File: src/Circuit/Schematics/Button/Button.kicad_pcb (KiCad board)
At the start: 2 copper layers, 17 x 15 mm, 5 parts, among them K1 CONN_3, SW1 SW_PUSH

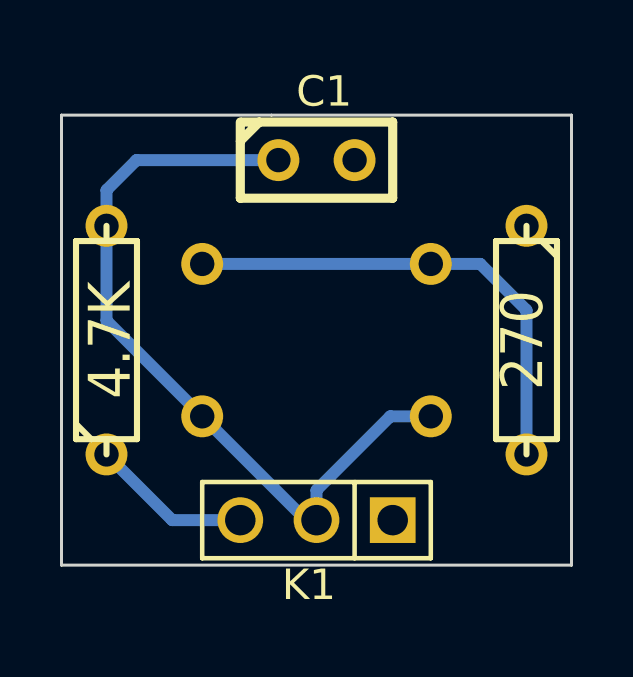
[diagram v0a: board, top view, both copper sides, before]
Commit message: Initial LED driver circuit
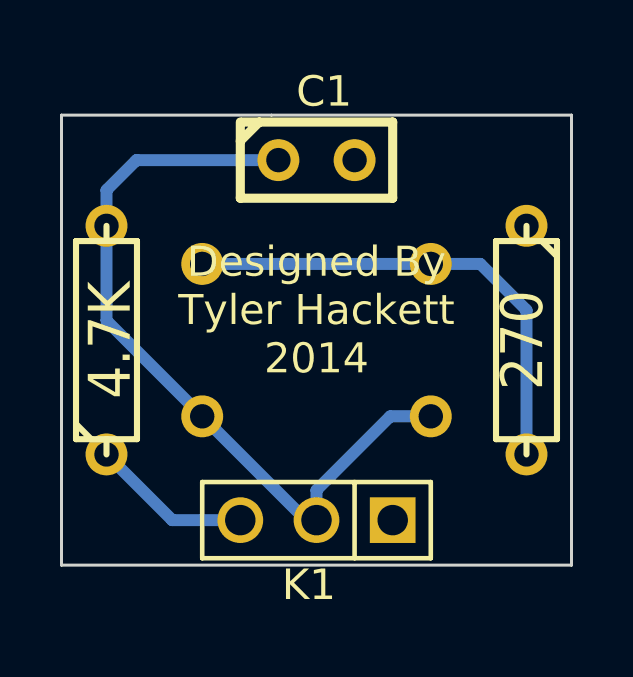
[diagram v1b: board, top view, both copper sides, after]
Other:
- board text added: "Designed By Tyler Hackett 2014"
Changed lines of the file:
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@@
     (links 9)
     (no_connects 0)
-    (area 195.449999 131.8504 221.962401 149.9972)
+    (area 195.449999 131.8504 212.550001 149.9972)
     (thickness 1.6)
-    (drawings 5)
+    (drawings 6)
     (tracks 16)
     (zones 0)
@@
     )
   )
+  (gr_text "Designed By\nTyler Hackett\n2014" (at 204 140) (layer F.SilkS)
+    (effects (font (size 1 1) (thickness 0.25)))
+  )
   (gr_line (start 212.5 133.5) (end 202.5 133.5) (angle 90) (layer Edge.Cuts) (width 0.1))
